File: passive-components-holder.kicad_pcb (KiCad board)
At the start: 2 copper layers, 100 parts

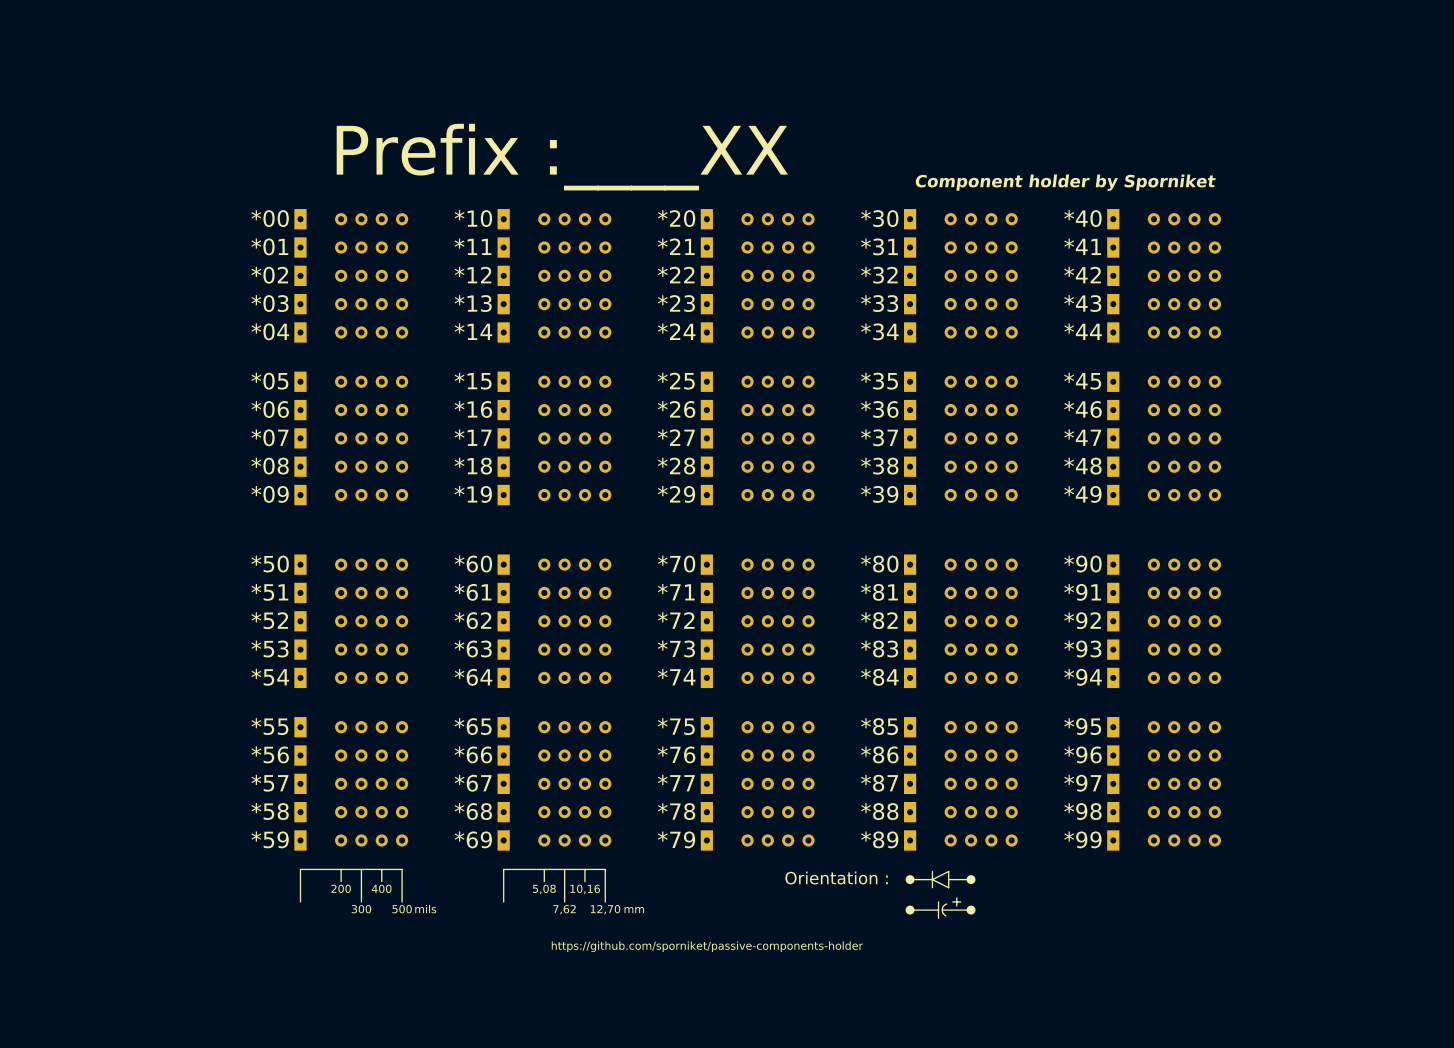
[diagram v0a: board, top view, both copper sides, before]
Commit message: finished v1 : mounting holes, outline shape, tweak orientation description
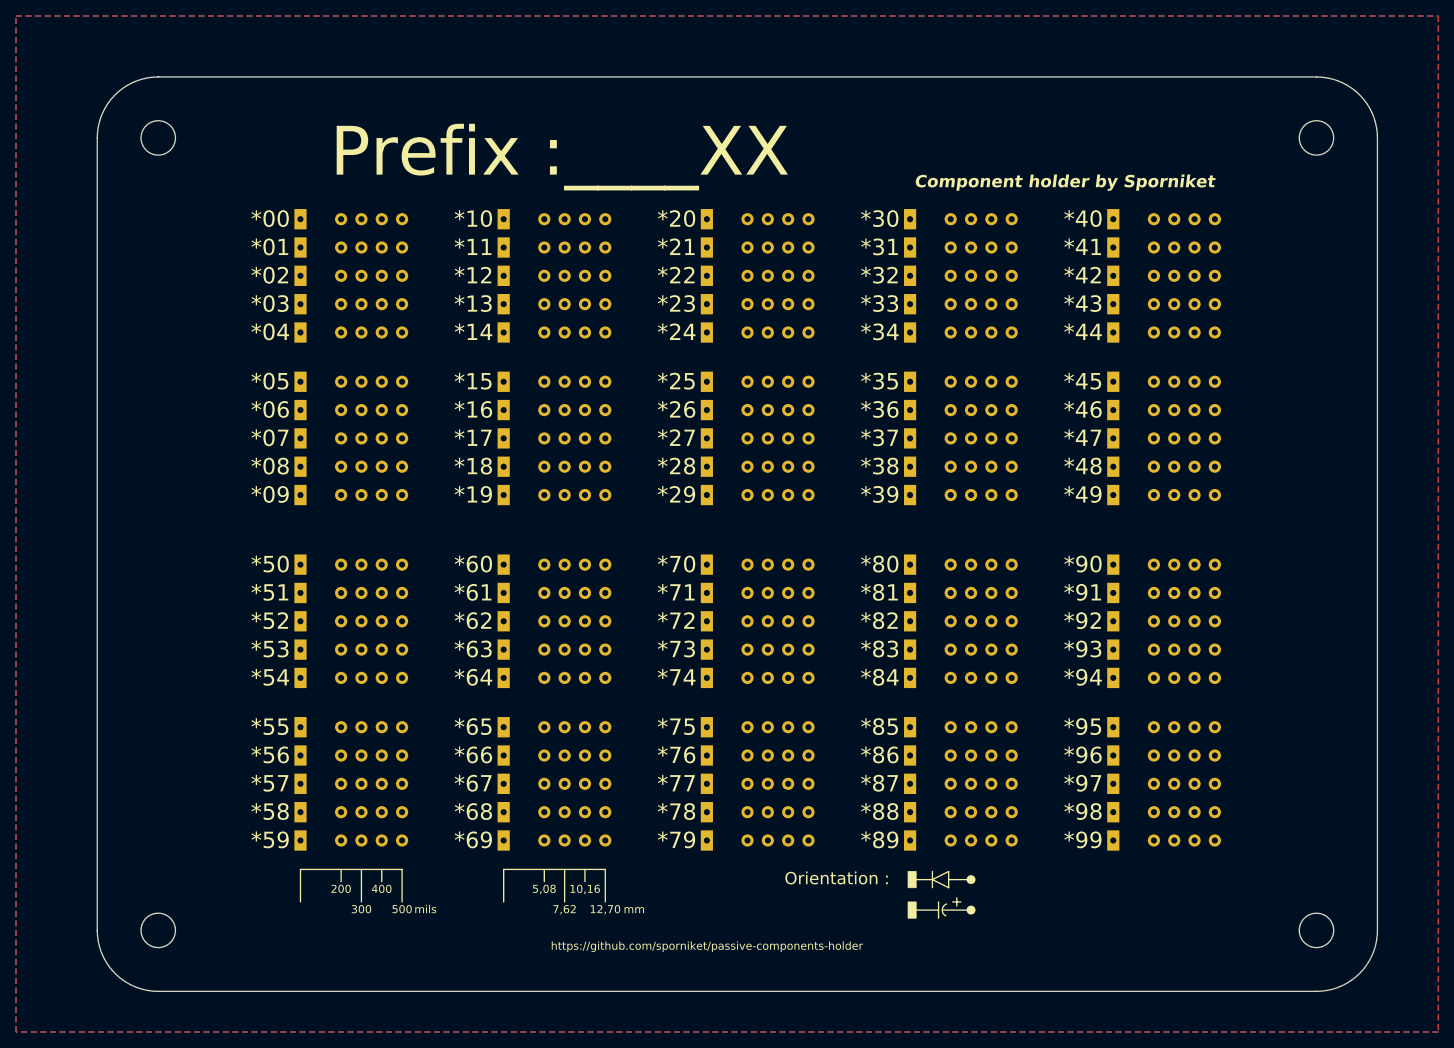
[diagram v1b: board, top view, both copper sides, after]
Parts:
- added H1: M4, MountingHole:MountingHole_4.3mm_M4, F.Cu at (83.8, 40.6)
- added H2: M4, MountingHole:MountingHole_4.3mm_M4, F.Cu at (228.6, 40.6)
- added H3: M4, MountingHole:MountingHole_4.3mm_M4, F.Cu at (228.6, 139.7)
- added H4: M4, MountingHole:MountingHole_4.3mm_M4, F.Cu at (83.8, 139.7)
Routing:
- added copper zone on B.Cu, net (none)
- added copper zone on F.Cu, net (none)
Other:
- board outline added: 160 x 114.3 mm
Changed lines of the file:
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@@
   )
   (paper "A4")
+  (title_block
+    (title "Passive components holder")
+    (date "2024-05-05")
+    (rev "v1.0.0")
+    (company "Sporniket")
+    (comment 3 "https://github.com/sporniket/passive-components-holder")
+    (comment 4 "Original repository")
+  )
   (layers
     (0 "F.Cu" signal)
@@
       (net 44 "unconnected-(*21-Pad2)") (pintype "passive"))
   )
+  (footprint "MountingHole:MountingHole_4.3mm_M4" (layer "F.Cu")
+    (at 228.6 139.7)
+    (descr "Mounting Hole 4.3mm, no annular, M4")
+    (tags "mounting hole 4.3mm no annular m4")
+    (property "Sheetfile" "passive-components-holder.kicad_sch")
+    (property "Sheetname" "")
+    (property "ki_description" "Mounting Hole without connection")
+    (property "ki_keywords" "mounting hole")
+    (attr exclude_from_pos_files)
+    (fp_text reference "H3" (at 0 -5.3) (layer "Dwgs.User")
+        (effects (font (size 1 1) (thickness 0.15)))
+    )
+    (fp_text value "M4" (at 0 5.3) (layer "F.Fab")
+        (effects (font (size 1 1) (thickness 0.15)))
+    )
+    (fp_text user "${REFERENCE}" (at 0 0) (layer "F.Fab")
+        (effects (font (size 1 1) (thickness 0.15)))
+    )
+    (fp_circle (center 0 0) (end 4.3 0)
+      (stroke (width 0.15) (type solid)) (fill none) (layer "Cmts.User"))
+    (fp_circle (center 0 0) (end 4.55 0)
+      (stroke (width 0.05) (type solid)) (fill none) (layer "F.CrtYd"))
+    (pad "" np_thru_hole circle (at 0 0) (size 4.3 4.3) (drill 4.3) (layers "*.Cu" "*.Mask"))
+  )
   (footprint "component_holder:component_holder_THT_pitches_200_300_400_500_mils" (layer "F.Cu")
     (at 101.6 57.88)
@@
       (net 32 "unconnected-(*15-Pad2)") (pintype "passive"))
   )
+  (footprint "MountingHole:MountingHole_4.3mm_M4" (layer "F.Cu")
+    (at 83.82 139.7)
+    (descr "Mounting Hole 4.3mm, no annular, M4")
+    (tags "mounting hole 4.3mm no annular m4")
+    (property "Sheetfile" "passive-components-holder.kicad_sch")
+    (property "Sheetname" "")
+    (property "ki_description" "Mounting Hole without connection")
+    (property "ki_keywords" "mounting hole")
+    (attr exclude_from_pos_files)
+    (fp_text reference "H4" (at 0 -5.3) (layer "Dwgs.User")
+        (effects (font (size 1 1) (thickness 0.15)))
+    )
+    (fp_text value "M4" (at 0 5.3) (layer "F.Fab")
+        (effects (font (size 1 1) (thickness 0.15)))
+    )
+    (fp_text user "${REFERENCE}" (at 0 0) (layer "F.Fab")
+        (effects (font (size 1 1) (thickness 0.15)))
+    )
+    (fp_circle (center 0 0) (end 4.3 0)
+      (stroke (width 0.15) (type solid)) (fill none) (layer "Cmts.User"))
+    (fp_circle (center 0 0) (end 4.55 0)
+      (stroke (width 0.05) (type solid)) (fill none) (layer "F.CrtYd"))
+    (pad "" np_thru_hole circle (at 0 0) (size 4.3 4.3) (drill 4.3) (layers "*.Cu" "*.Mask"))
+  )
   (footprint "component_holder:component_holder_THT_pitches_200_300_400_500_mils" (layer "F.Cu")
     (at 203.2 93.98)
@@
       (net 40 "unconnected-(*19-Pad2)") (pintype "passive"))
   )
+  (footprint "MountingHole:MountingHole_4.3mm_M4" (layer "F.Cu")
+    (at 228.6 40.64)
+    (descr "Mounting Hole 4.3mm, no annular, M4")
+    (tags "mounting hole 4.3mm no annular m4")
+    (property "Sheetfile" "passive-components-holder.kicad_sch")
+    (property "Sheetname" "")
+    (property "ki_description" "Mounting Hole without connection")
+    (property "ki_keywords" "mounting hole")
+    (attr exclude_from_pos_files)
+    (fp_text reference "H2" (at 0 -5.3) (layer "Dwgs.User")
+        (effects (font (size 1 1) (thickness 0.15)))
+    )
+    (fp_text value "M4" (at 0 5.3) (layer "F.Fab")
+        (effects (font (size 1 1) (thickness 0.15)))
+    )
+    (fp_text user "${REFERENCE}" (at 0 0) (layer "F.Fab")
+        (effects (font (size 1 1) (thickness 0.15)))
+    )
+    (fp_circle (center 0 0) (end 4.3 0)
+      (stroke (width 0.15) (type solid)) (fill none) (layer "Cmts.User"))
+    (fp_circle (center 0 0) (end 4.55 0)
+      (stroke (width 0.05) (type solid)) (fill none) (layer "F.CrtYd"))
+    (pad "" np_thru_hole circle (at 0 0) (size 4.3 4.3) (drill 4.3) (layers "*.Cu" "*.Mask"))
+  )
   (footprint "component_holder:component_holder_THT_pitches_200_300_400_500_mils" (layer "F.Cu")
     (at 127 114.3)
@@
     (pad "2" thru_hole circle (at 12.7 0) (size 1.524 1.524) (drill 0.762) (layers "*.Cu" "*.Mask")
       (net 122 "unconnected-(*60-Pad2)") (pintype "passive"))
+  )
+  (footprint "MountingHole:MountingHole_4.3mm_M4" (layer "F.Cu")
+    (at 83.82 40.64)
+    (descr "Mounting Hole 4.3mm, no annular, M4")
+    (tags "mounting hole 4.3mm no annular m4")
+    (property "Sheetfile" "passive-components-holder.kicad_sch")
+    (property "Sheetname" "")
+    (property "ki_description" "Mounting Hole without connection")
+    (property "ki_keywords" "mounting hole")
+    (attr exclude_from_pos_files)
+    (fp_text reference "H1" (at 0 -5.3) (layer "Dwgs.User")
+        (effects (font (size 1 1) (thickness 0.15)))
+    )
+    (fp_text value "M4" (at 0 5.3) (layer "F.Fab")
+        (effects (font (size 1 1) (thickness 0.15)))
+    )
+    (fp_text user "${REFERENCE}" (at 0 0) (layer "F.Fab")
+        (effects (font (size 1 1) (thickness 0.15)))
+    )
+    (fp_circle (center 0 0) (end 4.3 0)
+      (stroke (width 0.15) (type solid)) (fill none) (layer "Cmts.User"))
+    (fp_circle (center 0 0) (end 4.55 0)
+      (stroke (width 0.05) (type solid)) (fill none) (layer "F.CrtYd"))
+    (pad "" np_thru_hole circle (at 0 0) (size 4.3 4.3) (drill 4.3) (layers "*.Cu" "*.Mask"))
   )
   (gr_line (start 182.626 134.366) (end 180.594 133.35)
@@
   (gr_line (start 134.62 132.08) (end 134.62 136.144)
     (stroke (width 0.1) (type default)) (layer "F.SilkS"))
-  (gr_circle (center 177.8 137.16) (end 178.308 137.16)
-    (stroke (width 0.1) (type solid)) (fill solid) (layer "F.SilkS"))
   (gr_line (start 132.08 132.08) (end 132.08 133.604)
     (stroke (width 0.1) (type default)) (layer "F.SilkS"))
@@
   (gr_line (start 178.054 137.16) (end 181.356 137.16)
     (stroke (width 0.1) (type default)) (layer "F.SilkS"))
+  (gr_rect (start 177.546 132.334) (end 178.562 134.366)
+    (stroke (width 0.1) (type solid)) (fill solid) (layer "F.SilkS"))
   (gr_line (start 101.6 132.08) (end 114.3 132.08)
     (stroke (width 0.1) (type default)) (layer "F.SilkS"))
+  (gr_rect (start 177.546 136.144) (end 178.562 138.176)
+    (stroke (width 0.1) (type solid)) (fill solid) (layer "F.SilkS"))
   (gr_line (start 127 132.08) (end 139.7 132.08)
     (stroke (width 0.1) (type default)) (layer "F.SilkS"))
@@
   (gr_arc (start 182.26679 137.87842) (mid 181.824803 137.103061) (end 182.372 136.398)
     (stroke (width 0.1) (type default)) (layer "F.SilkS"))
-  (gr_circle (center 177.8 133.35) (end 178.308 133.35)
-    (stroke (width 0.1) (type solid)) (fill solid) (layer "F.SilkS"))
   (gr_line (start 139.7 132.08) (end 139.7 136.144)
     (stroke (width 0.1) (type default)) (layer "F.SilkS"))
   (gr_line (start 114.3 132.08) (end 114.3 136.144)
     (stroke (width 0.1) (type default)) (layer "F.SilkS"))
+  (gr_line (start 76.2 40.64) (end 76.2 139.7)
+    (stroke (width 0.05) (type default)) (layer "Edge.Cuts"))
+  (gr_arc (start 76.2 40.64) (mid 78.431846 35.251846) (end 83.82 33.02)
+    (stroke (width 0.05) (type default)) (layer "Edge.Cuts"))
+  (gr_line (start 236.22 139.7) (end 236.22 40.64)
+    (stroke (width 0.05) (type default)) (layer "Edge.Cuts"))
+  (gr_line (start 228.6 33.02) (end 83.82 33.02)
+    (stroke (width 0.05) (type default)) (layer "Edge.Cuts"))
+  (gr_arc (start 228.6 33.02) (mid 233.988154 35.251846) (end 236.22 40.64)
+    (stroke (width 0.05) (type default)) (layer "Edge.Cuts"))
+  (gr_line (start 83.82 147.32) (end 228.6 147.32)
+    (stroke (width 0.05) (type default)) (layer "Edge.Cuts"))
+  (gr_arc (start 236.22 139.7) (mid 233.988154 145.088154) (end 228.6 147.32)
+    (stroke (width 0.05) (type default)) (layer "Edge.Cuts"))
+  (gr_arc (start 83.82 147.32) (mid 78.431846 145.088154) (end 76.2 139.7)
+    (stroke (width 0.05) (type default)) (layer "Edge.Cuts"))
   (gr_text "400" (at 111.76 135.128) (layer "F.SilkS")
     (effects (font (size 1 1) (thickness 0.1)) (justify bottom))
@@
     (effects (font (size 1 1) (thickness 0.1)) (justify left bottom))
   )
+  (zone (net 0) (net_name "") (layers "F&B.Cu") (hatch edge 0.5)
+    (connect_pads (clearance 0.5))
+    (min_thickness 0.25) (filled_areas_thickness no)
+    (fill yes (thermal_gap 0.5) (thermal_bridge_width 0.5) (island_removal_mode 1) (island_area_min 10))
+    (polygon
+      (pts
+        (xy 66.04 25.4)
+        (xy 243.84 25.4)
+        (xy 243.84 152.4)
+        (xy 66.04 152.4)
+      )
+    )
+  )
   (group "" (id 105df4be-7172-4e81-805e-144bd0c22342)
